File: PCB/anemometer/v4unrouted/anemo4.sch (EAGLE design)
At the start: 66 parts, among them IC1 AD8223, IC2 AD8223, IC3 AD8223, IC4 AD8223, IC6 TL072D, J1 RJ12STRAIGHT-I2C, J2 RJ12STRAIGHT-I2C

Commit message: put all devices on one side on integrated bertha
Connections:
- net GND renamed AGND
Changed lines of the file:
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@@
 </segment>
 </net>
-<net name="GND" class="1">
+<net name="AGND" class="1">
 <segment>
 <pinref part="DIV2" gate="G$1" pin="1"/>

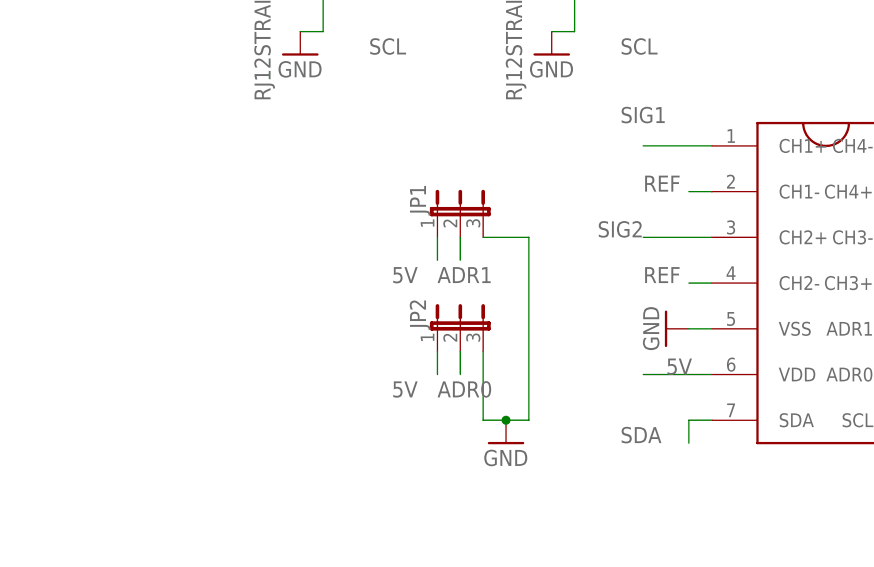
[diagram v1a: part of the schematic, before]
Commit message: routed anemometer and integrated bertha with ground planes and separate analog and digital ground. ready for fabrication
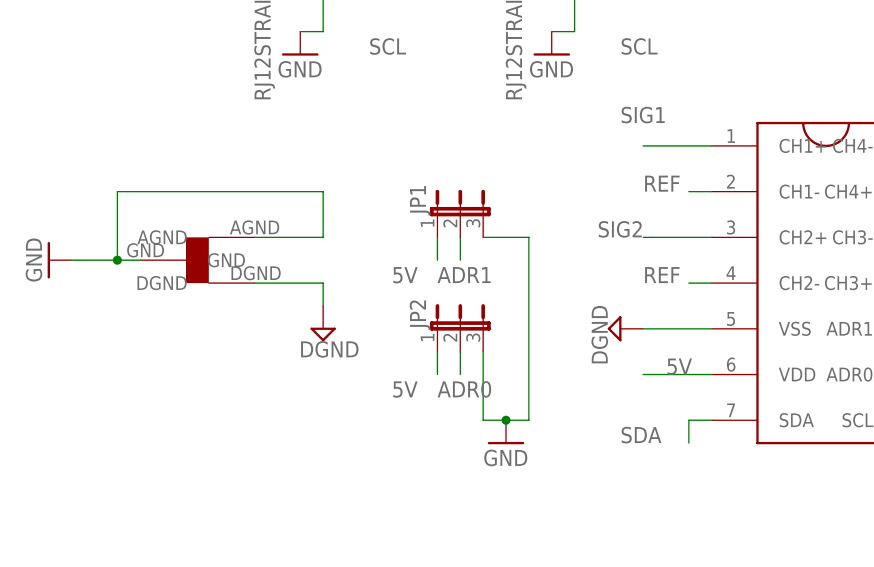
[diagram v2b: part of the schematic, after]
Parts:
- added U$2: STARGND, lpatiny:STARGND
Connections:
- removed net AGND: C1.2, C2.2, C3.2, C4.2, C5.2, CF1.1, CF2.1, CF3.1, CF4.1, C_MCP1.1, C_MCP3424.1, C_TL072.1, DIV2.1, DIV4.1, DIV6.1, DIV8.1, IC1.-V, IC2.-V, IC3.-V, IC4.-V, IC6P.V-, J1.4, J1.6, J2.4, J2.6, JP1.3, JP2.3, LED0.C, PT100_1.1, PT100_2.1, PT100_3.1, PT100_4.1, PT1K_1.1, PT1K_2.1, PT1K_3.1, PT1K_4.1, REF2.1, U$1.VSS
- new net DGND: U$1.VSS, U$2.DGND
- new net GND: C1.2, C2.2, C3.2, C4.2, C5.2, CF1.1, CF2.1, CF3.1, CF4.1, C_MCP1.1, C_MCP3424.1, C_TL072.1, DIV2.1, DIV4.1, DIV6.1, DIV8.1, IC1.-V, IC2.-V, IC3.-V, IC4.-V, IC6P.V-, J1.4, J1.6, J2.4, J2.6, JP1.3, JP2.3, LED0.C, PT100_1.1, PT100_2.1, PT100_3.1, PT100_4.1, PT1K_1.1, PT1K_2.1, PT1K_3.1, PT1K_4.1, REF2.1, U$2.AGND, U$2.GND
